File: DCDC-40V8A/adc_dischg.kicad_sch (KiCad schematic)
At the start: 12 parts, among them Q10 2N7002, Q11 2N7002, Q12 2N7002, Q5 2N7002, Q6 2N7002, Q7 2N7002, Q8 2N7002, Q9 2N7002, U10 CD4051B, U17 74HC595

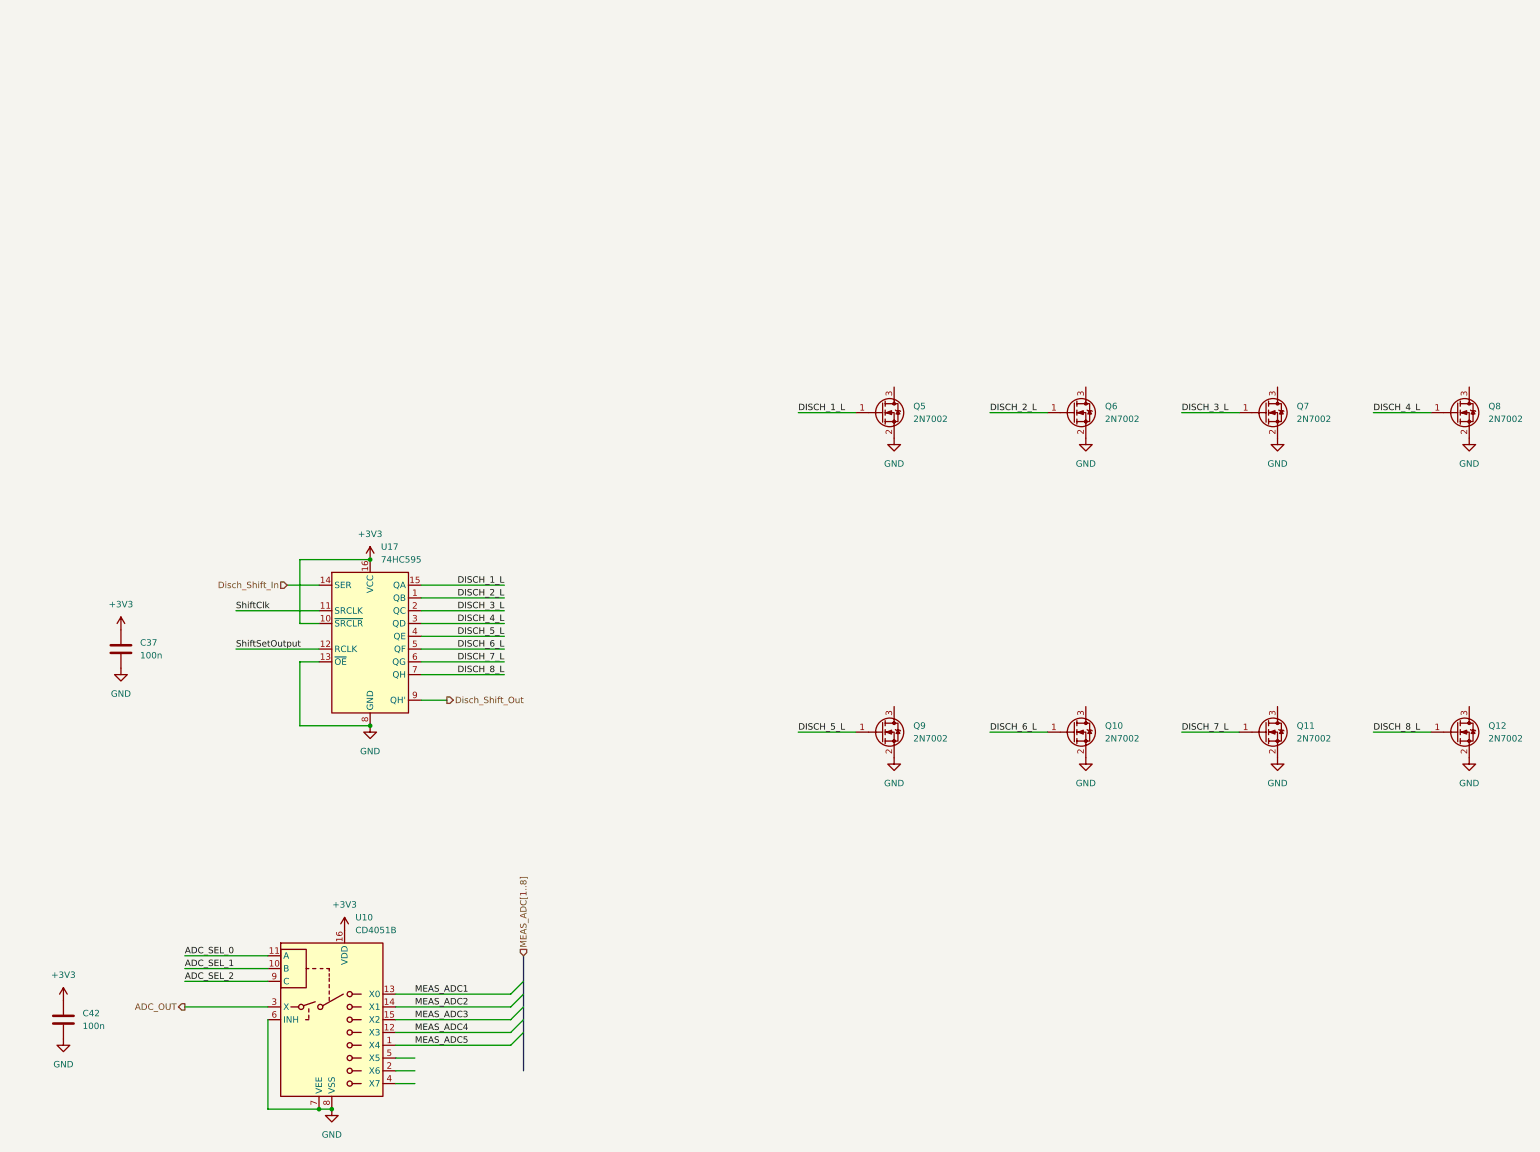
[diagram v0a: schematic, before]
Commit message: added discharge circuitry and help texts
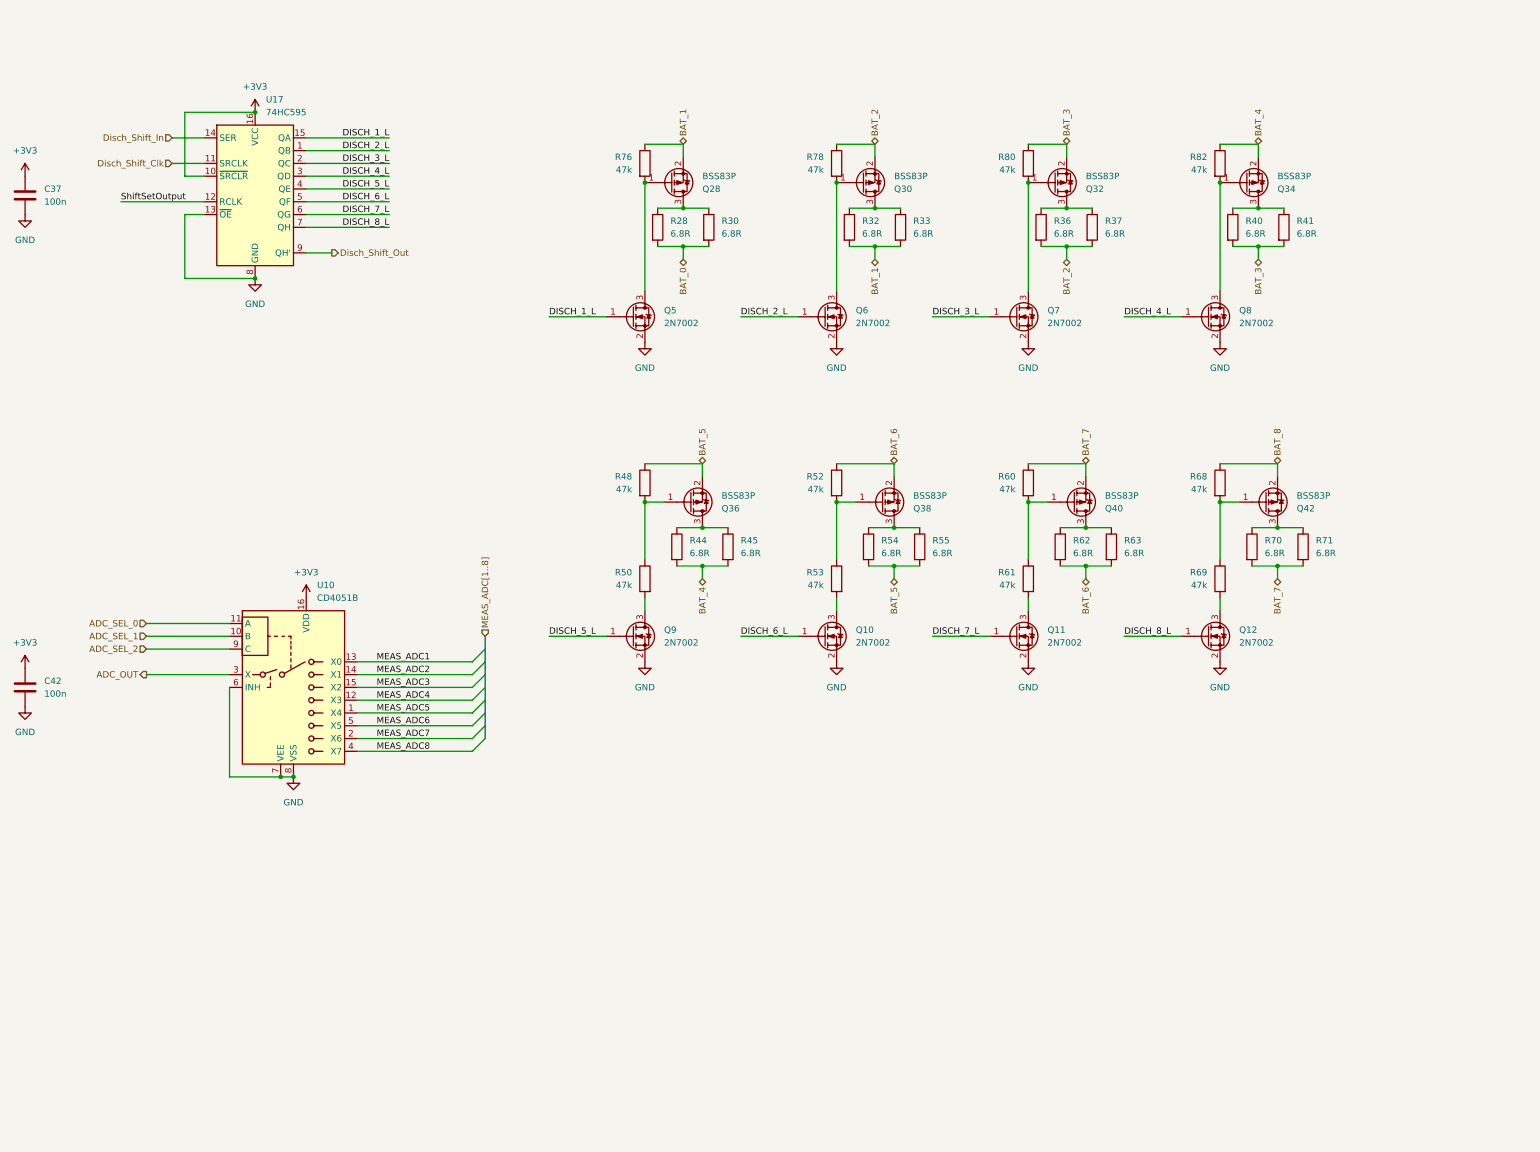
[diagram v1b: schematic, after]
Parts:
- added Q28, Q30, Q32, Q34, Q36, Q38, Q40, Q42: BSS83P, Package_TO_SOT_SMD:SOT-23, symbol Transistor_FET:BSS83P
- added R28, R30, R32, R33, R36, R37, R40, R41, R44, R45, R54, R55, R62, R63, R70, R71: 6.8R, Resistor_SMD:R_2010_5025Metric, symbol Device:R
- added R48, R50, R52, R53, R60, R61, R68, R69, R76, R78, R80, R82: 47k, Resistor_SMD:R_0603_1608Metric, symbol Device:R
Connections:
- net at Q10.3 (D): now also R53.2
- net at Q7.3 (D): now also Q32.1 (G), R80.2
- net at Q6.3 (D): now also Q30.1 (G), R78.2
- net at Q9.3 (D): now also R50.2
- net at Q5.3 (D): now also Q28.1 (G), R76.2
- net at Q8.3 (D): now also Q34.1 (G), R82.2
- net at Q12.3 (D): now also R69.2
- net MEAS_ADC7: now reaches U10.2 (X6)
- net MEAS_ADC8: now reaches U10.4 (X7)
- net MEAS_ADC6: now reaches U10.5 (X5)
- net at Q11.3 (D): now also R61.2
- net ShiftClk renamed Disch_Shift_Clk
- new net: Q40.1 (G), R60.2, R61.1
- new net: Q36.1 (G), R48.2, R50.1
- new net: Q36.3 (D), R44.1, R45.1
- new net: Q30.3 (D), R32.1, R33.1
- new net: Q42.1 (G), R68.2, R69.1
- new net: Q38.1 (G), R52.2, R53.1
- new net: Q42.3 (D), R70.1, R71.1
- new net: Q40.3 (D), R62.1, R63.1
- new net: Q38.3 (D), R54.1, R55.1
- new net: Q28.3 (D), R28.1, R30.1
- new net: Q34.3 (D), R40.1, R41.1
- new net: Q32.3 (D), R36.1, R37.1
- new net BAT_0: R28.2, R30.2
- new net BAT_1: Q28.2 (S), R32.2, R33.2, R76.1
- new net BAT_2: Q30.2 (S), R36.2, R37.2, R78.1
- new net BAT_3: Q32.2 (S), R40.2, R41.2, R80.1
- new net BAT_4: Q34.2 (S), R44.2, R45.2, R82.1
- new net BAT_5: Q36.2 (S), R48.1, R54.2, R55.2
- new net BAT_6: Q38.2 (S), R52.1, R62.2, R63.2
- new net BAT_7: Q40.2 (S), R60.1, R70.2, R71.2
- new net BAT_8: Q42.2 (S), R68.1
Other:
- moved on the sheet: C37, C42, Q10, Q11, Q12, Q5, Q6, Q7, Q8, Q9, U10, U17

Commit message: wip
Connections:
- net ADC_OUT renamed ADC_OUT_L
- net MEAS_ADC1 renamed MEAS_L1
- net MEAS_ADC2 renamed MEAS_L2
- net MEAS_ADC3 renamed MEAS_L3
- net MEAS_ADC4 renamed MEAS_L4
- net MEAS_ADC5 renamed MEAS_L5
- net MEAS_ADC6 renamed MEAS_L6
- net MEAS_ADC7 renamed MEAS_L7
- net MEAS_ADC8 renamed MEAS_L8
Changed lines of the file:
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@@
 	(generator_version "10.0")
 	(paper "A4")
+	(text_box "TODO: Search better PMOS"
+		(exclude_from_sim no)
+		(at 199.39 15.24 0)
+		(size 24.13 17.78)
+		(margins 0.9525 0.9525 0.9525 0.9525)
+		(stroke
+			(width 0)
+			(type solid)
+		)
+		(fill
+			(type none)
+		)
+		(effects
+			(font
+				(size 1.27 1.27)
+			)
+			(justify left top)
+		)
+	)
 	(junction
 		(at 227.33 62.23)
@@
 		)
 	)
-	(label "MEAS_ADC7"
+	(label "MEAS_L7"
 		(at 90.17 160.02 0)
 		(effects
@@
 		)
 	)
-	(label "MEAS_ADC5"
+	(label "MEAS_L5"
 		(at 90.17 154.94 0)
 		(effects
@@
 		)
 	)
-	(label "MEAS_ADC8"
+	(label "MEAS_L8"
 		(at 90.17 162.56 0)
 		(effects
@@
 		)
 	)
-	(label "MEAS_ADC6"
+	(label "MEAS_L6"
 		(at 90.17 157.48 0)
 		(effects
@@
 		)
 	)
-	(label "MEAS_ADC4"
+	(label "MEAS_L4"
 		(at 90.17 152.4 0)
 		(effects
@@
 		)
 	)
-	(label "MEAS_ADC3"
+	(label "MEAS_L3"
 		(at 90.17 149.86 0)
 		(effects
@@
 		)
 	)
-	(label "MEAS_ADC1"
+	(label "MEAS_L1"
 		(at 90.17 144.78 0)
 		(effects
@@
 		)
 	)
-	(label "MEAS_ADC2"
+	(label "MEAS_L2"
 		(at 90.17 147.32 0)
 		(effects
@@
 		)
 	)
-	(hierarchical_label "MEAS_ADC[1..8]"
+	(hierarchical_label "MEAS_L[1..8]"
 		(shape input)
 		(at 111.76 139.7 90)
@@
 		)
 	)
-	(hierarchical_label "ADC_OUT"
+	(hierarchical_label "ADC_OUT_L"
 		(shape output)
 		(at 44.45 147.32 180)

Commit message: renumbering
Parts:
- renumbered C37 to C41, Q28 to Q14, Q30 to Q15, Q32 to Q16, Q34 to Q17, Q5 to Q18, Q6 to Q19, Q7 to Q20, Q8 to Q21, Q36 to Q22, Q38 to Q23, Q40 to Q24, Q42 to Q25, Q9 to Q26, Q10 to Q27, Q11 to Q28, Q12 to Q29, R76 to R41, R78 to R42, R80 to R43, R82 to R44, R28 to R45, R30 to R46, R32 to R47, R33 to R48, R36 to R49, R37 to R50, R40 to R51, R41 to R52, R48 to R53, R52 to R54, R60 to R55, R68 to R56, R44 to R57, R45 to R58, R54 to R59, R55 to R60, R62 to R61, R63 to R62, R70 to R63, R71 to R64, R50 to R65, R53 to R66, R61 to R67, R69 to R68, U17 to U10, U10 to U11
